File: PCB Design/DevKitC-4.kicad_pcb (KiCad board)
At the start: 2 copper layers, 86.9 x 63.7 mm, 18 parts, among them J1 Screw_Terminal_01x02, J2 Screw_Terminal_01x02, J3 Screw_Terminal_01x04, J5 Screw_Terminal_01x03, Q1 IRFZ44N, SW1 SW_DPDT_x2, U1 ESP32-DevKitC, U2 Generic_5v_Module

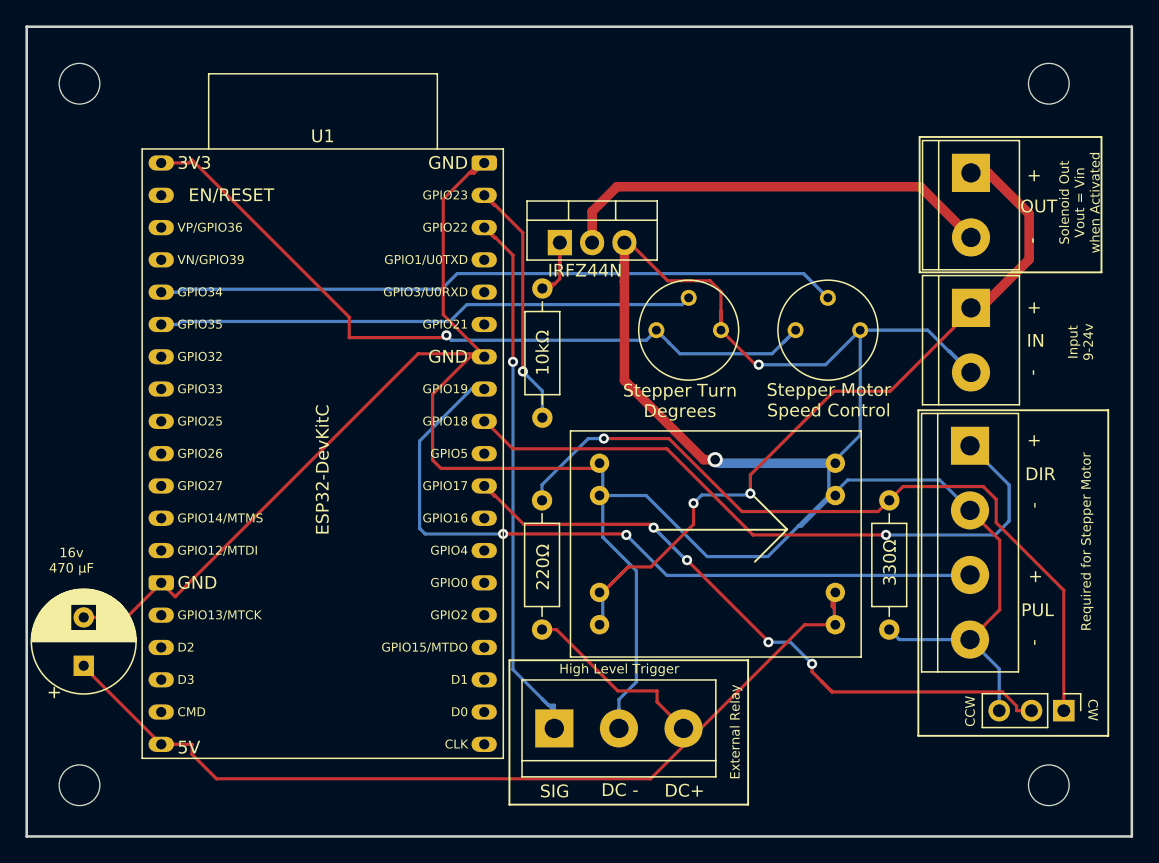
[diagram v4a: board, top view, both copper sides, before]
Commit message: Squashed commit of the following:
commit 8d3ad245b0b0885bf609d6c80dccf06c404355da
Author: Scott Dial <smdial@alumni.purdue.edu>
Date:   Sun Mar 26 20:17:48 2023 -0400

    updated pcb and arduino

commit aee9d78b6388df0d7588c47fb258c3b1a8245808
Author: Bullseye <90105099+100-5x@users.noreply.github.com>
Date:   Tue Feb 14 13:17:23 2023 -0500

    code changes.

    switched HIGH & LOW for the switch

commit 5ec61c4ec09789be3bb0214a7fa9b8cab35d8441
Author: Bullseye <90105099+100-5x@users.noreply.github.com>
Date:   Wed Feb 8 12:47:40 2023 -0500

    PCB Text Updates

commit 8f82cd768d246ead5170c5acd62d163460c6e75b
Author: Bullseye <90105099+100-5x@users.noreply.github.com>
Date:   Mon Feb 6 09:26:47 2023 -0500

    PCB & Code changes for version 2

    Added Diode to PCB
    Added Switch for Worker / Standalone
    Instructions on back silkscreen

commit 88eaa1f8307400ed63f43e3c574ed5baf0296be2
Author: Bullseye <90105099+100-5x@users.noreply.github.com>
Date:   Sun Jan 29 22:14:40 2023 -0500

    PCB and code changes for Dual Mode

commit 5d082f1582dbe39b2b10d9fe13ea9803484a0bf6
Author: Bullseye <90105099+100-5x@users.noreply.github.com>
Date:   Wed Jan 25 21:50:28 2023 -0600

    New file for dual work.
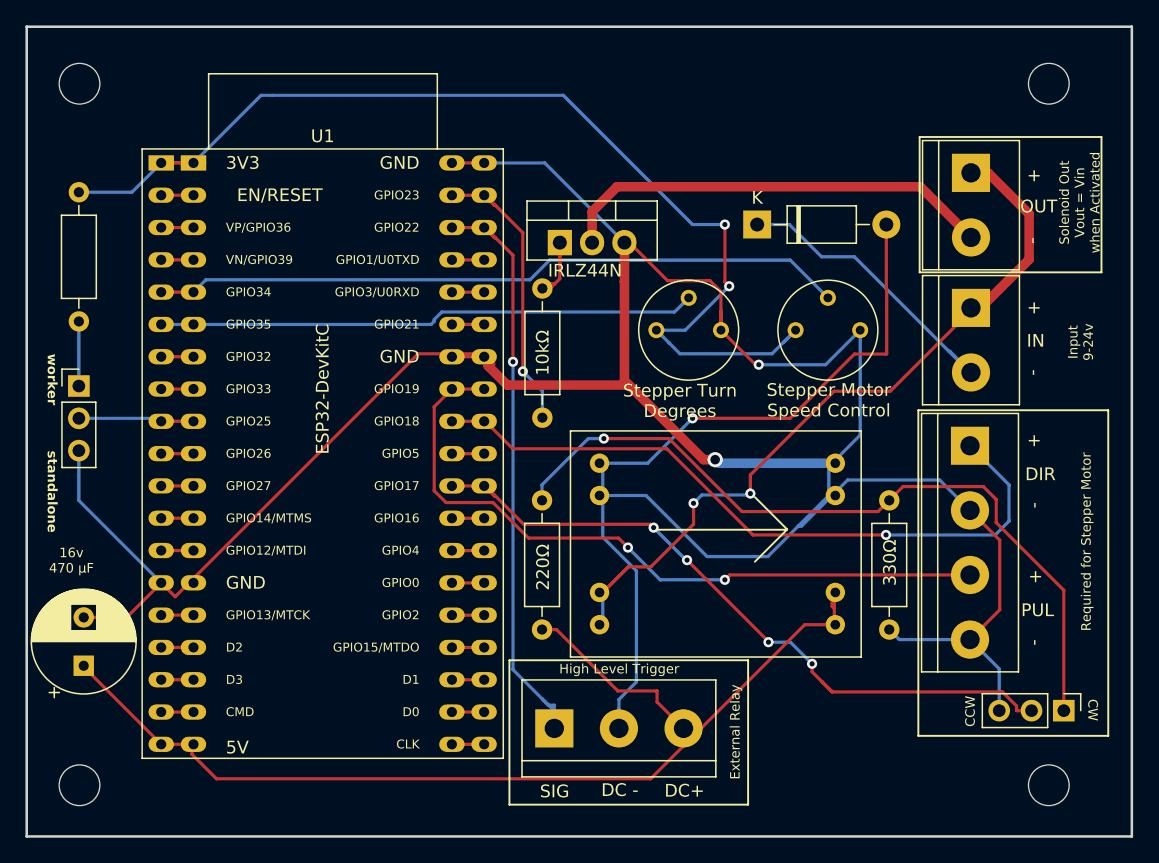
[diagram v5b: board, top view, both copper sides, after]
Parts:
- added D1: 1N5819, Diode_THT:D_DO-41_SOD81_P10.16mm_Horizontal, F.Cu at (116.8, 66.0)
- added R6: 1kΩ, Resistor_THT:R_Axial_DIN0207_L6.3mm_D2.5mm_P10.16mm_Horizontal, F.Cu at (63.5, 63.5)
- added SW2: SW_DPDT_x2, Connector_PinHeader_2.54mm:PinHeader_1x03_P2.54mm_Vertical, F.Cu at (63.5, 78.7)
- Q1: value IRFZ44N -> IRLZ44N
- U1: footprint ESP32_modules:ESP32-DevKitC -> Espressif:ESP32-Combined
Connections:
- U1 pad 9: unconnected-(U1-Pad9) -> Net-(SW2A-B)
- U2 pad 1: GND -> Net-(D1-A)
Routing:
- net Net-(D1-A): track 0.00 -> 36.3 mm, vias 0 -> 1
- net +3V3: track 59.5 -> 87.2 mm, vias 1 -> 2
- net GND: track 251.9 -> 264.7 mm
- net Net-(SW2A-B): track 0.00 -> 9.11 mm
- net Net-(SW2A-A): track 0.00 -> 5.08 mm
- net unconnected-(U1-SENSOR_VP/GPIO36/ADC1_CH0-Pad3): track 0.00 -> 2.54 mm
- net unconnected-(U1-SENSOR_VN/GPIO39/ADC1_CH3-Pad4): track 0.00 -> 2.54 mm
- net unconnected-(U1-SD_DATA3/GPIO10-Pad17): track 0.00 -> 2.54 mm
- net unconnected-(U1-SD_DATA2/GPIO9-Pad16): track 0.00 -> 2.54 mm
- net unconnected-(U1-MTMS/GPIO14/ADC2_CH6-Pad12): track 0.00 -> 2.54 mm
- net unconnected-(U1-MTCK/GPIO13/ADC2_CH4-Pad15): track 0.00 -> 2.54 mm
- net unconnected-(U1-DAC_2/ADC2_CH9/GPIO26-Pad10): track 0.00 -> 2.54 mm
- net unconnected-(U1-CMD-Pad18): track 0.00 -> 2.54 mm
- net unconnected-(U1-CHIP_PU-Pad2): track 0.00 -> 2.54 mm
- net unconnected-(U1-ADC2_CH7/GPIO27-Pad11): track 0.00 -> 2.54 mm
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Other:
- board text added: "Board Design 2.0"
- board text added: "Supply 9v-24v to INPUT connectors. If using a pass through to a linear actuator, connect OUTPUT +/- to your actuator. ** Voltage is the same as input. If using a stepper motor: Connect DIR+ & DIR- to the stepper motor driver ports with the same name. Connect PUL+ & PUL- to the stepper motor driver ports with the same name. If using an extenral relay: Use SIG to the INPUT of the relay. DC+ supplie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"
- board text added: "standalone"
- board text added: "worker"
- board text removed: "Board Design 1.9"
